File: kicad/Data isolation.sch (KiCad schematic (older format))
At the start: 0 parts

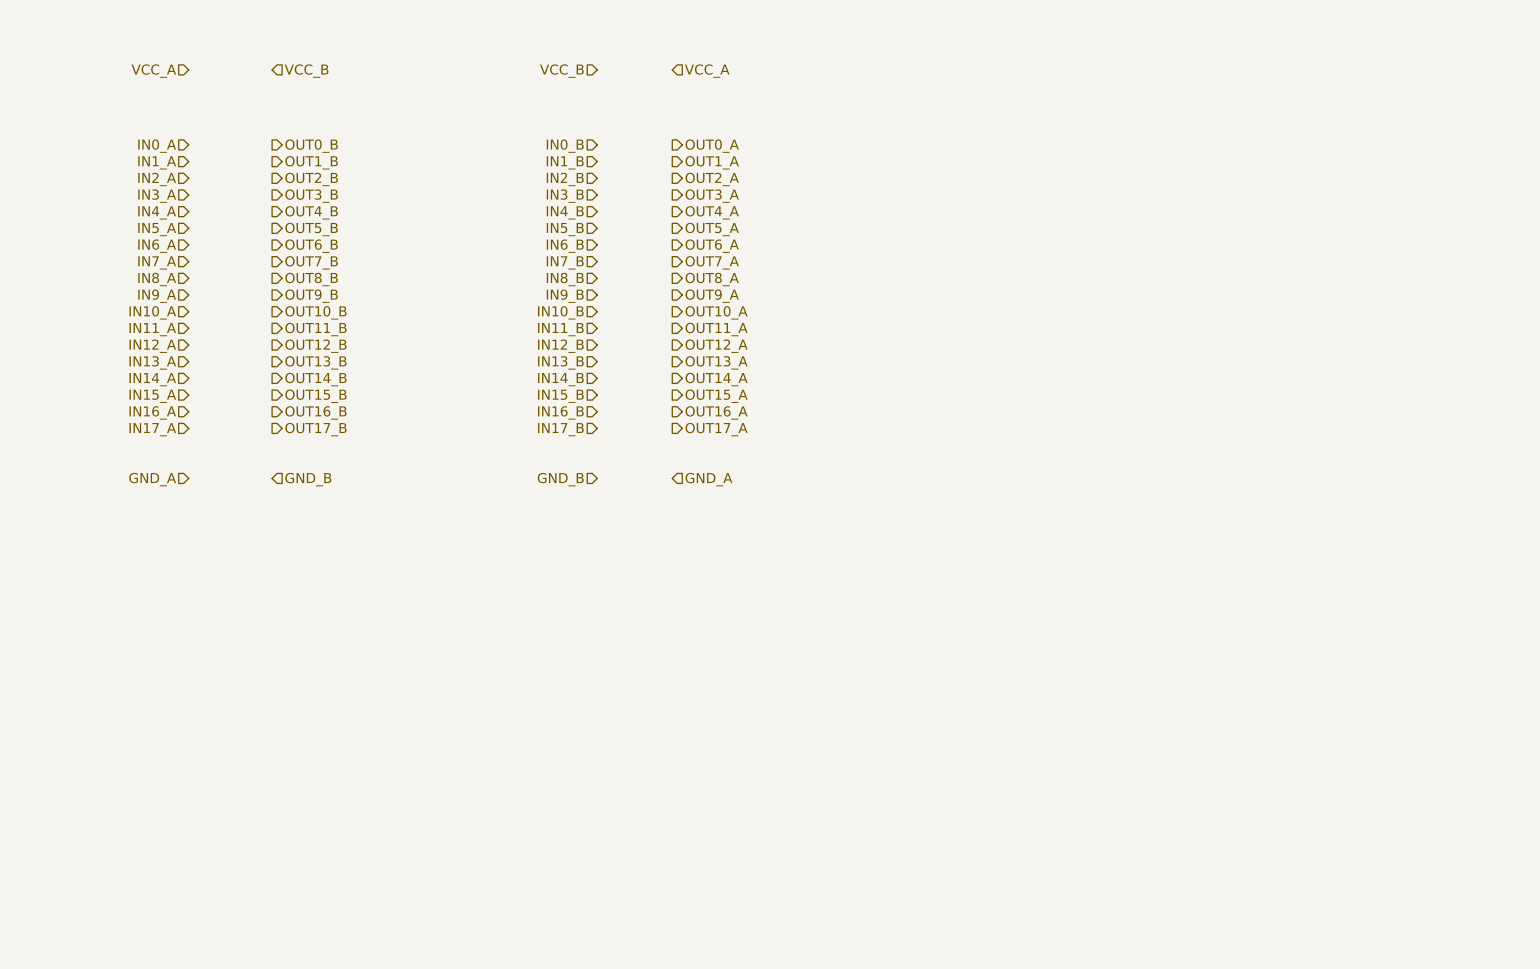
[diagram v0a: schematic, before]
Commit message: Completed data and power isolation sheets
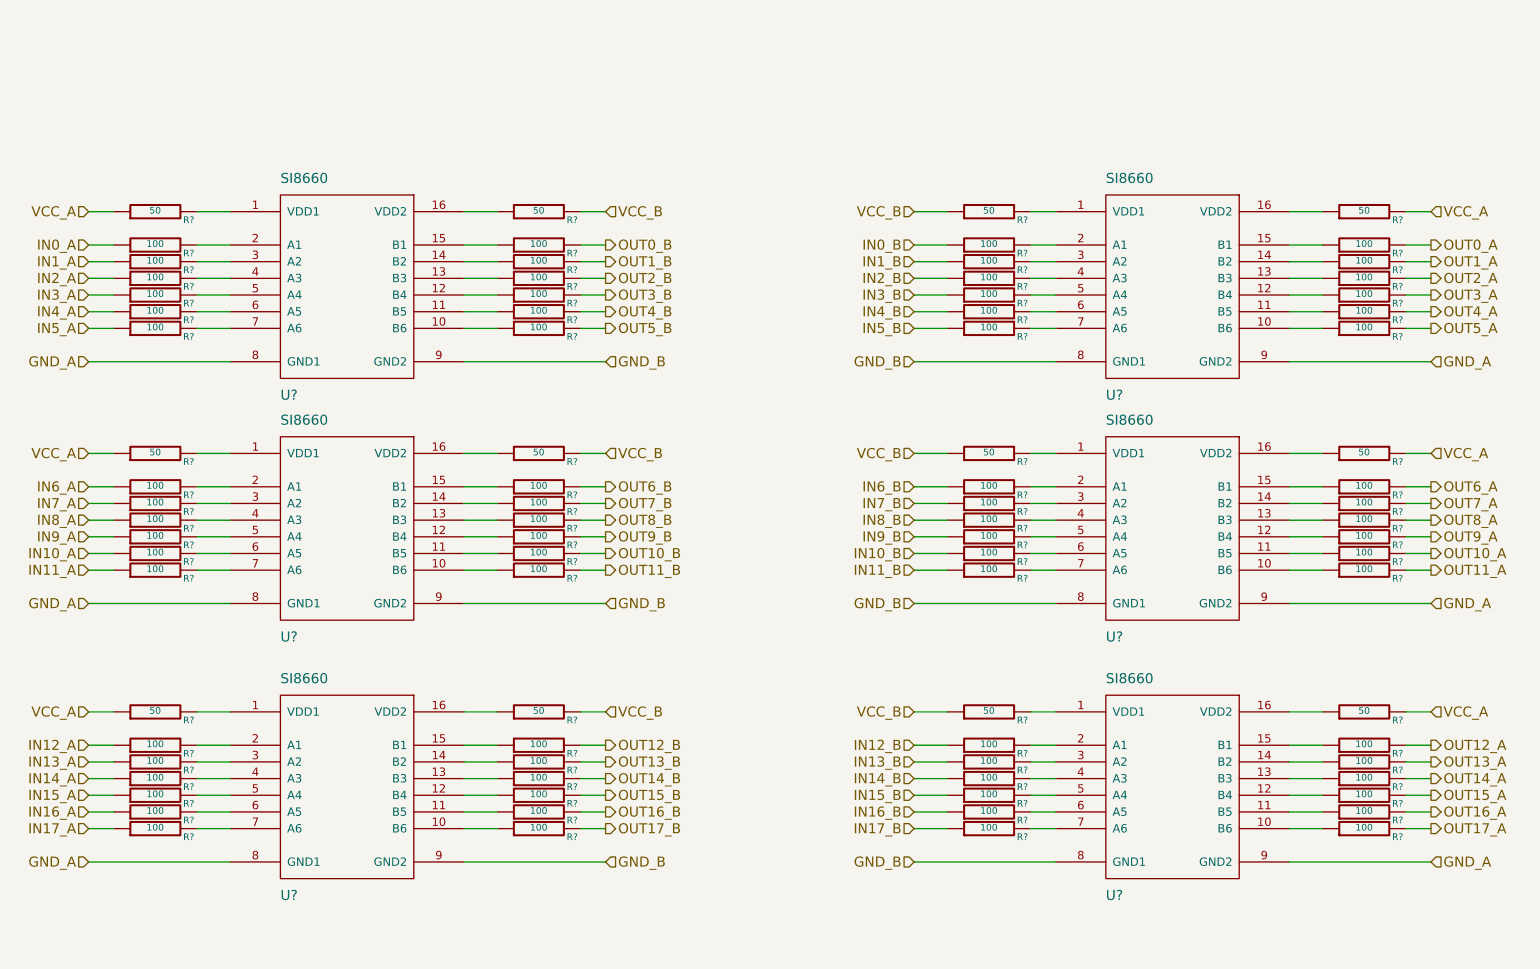
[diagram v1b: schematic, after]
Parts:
- added R? (x12): 50, ~, symbol R
- added R? (x72): 100, ~, symbol R
- added U? (x6): SI8660, ~, symbol SI8660
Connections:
- net GND_A: now also U?.8 (GND1), U?.8 (GND1), U?.8 (GND1), U?.9 (GND2), U?.9 (GND2), U?.9 (GND2)
- net GND_B: now also U?.8 (GND1), U?.8 (GND1), U?.8 (GND1), U?.9 (GND2), U?.9 (GND2), U?.9 (GND2)
- net IN0_A: now also R?.1
- net IN0_B: now also R?.1
- net IN10_A: now also R?.1
- net IN10_B: now also R?.1
- net IN11_A: now also R?.1
- net IN11_B: now also R?.1
- net IN12_A: now also R?.1
- net IN12_B: now also R?.1
- net IN13_A: now also R?.1
- net IN13_B: now also R?.1
- net IN14_A: now also R?.1
- net IN14_B: now also R?.1
- net IN15_A: now also R?.1
- net IN15_B: now also R?.1
- net IN16_A: now also R?.1
- net IN16_B: now also R?.1
- net IN17_A: now also R?.1
- net IN17_B: now also R?.1
- net IN1_A: now also R?.1
- net IN1_B: now also R?.1
- net IN2_A: now also R?.1
- net IN2_B: now also R?.1
- net IN3_A: now also R?.1
- net IN3_B: now also R?.1
- net IN4_A: now also R?.1
- net IN4_B: now also R?.1
- net IN5_A: now also R?.1
- net IN5_B: now also R?.1
- net IN6_A: now also R?.1
- net IN6_B: now also R?.1
- net IN7_A: now also R?.1
- net IN7_B: now also R?.1
- net IN8_A: now also R?.1
- net IN8_B: now also R?.1
- net IN9_A: now also R?.1
- net IN9_B: now also R?.1
- net OUT0_A: now also R?.2
- net OUT0_B: now also R?.2
- net OUT10_A: now also R?.2
- net OUT10_B: now also R?.2
- net OUT11_A: now also R?.2
- net OUT11_B: now also R?.2
- net OUT12_A: now also R?.2
- net OUT12_B: now also R?.2
- net OUT13_A: now also R?.2
- net OUT13_B: now also R?.2
- net OUT14_A: now also R?.2
- net OUT14_B: now also R?.2
- net OUT15_A: now also R?.2
- net OUT15_B: now also R?.2
- net OUT16_A: now also R?.2
- net OUT16_B: now also R?.2
- net OUT17_A: now also R?.2
- net OUT17_B: now also R?.2
- net OUT1_A: now also R?.2
- net OUT1_B: now also R?.2
- net OUT2_A: now also R?.2
- net OUT2_B: now also R?.2
- net OUT3_A: now also R?.2
- net OUT3_B: now also R?.2
- net OUT4_A: now also R?.2
- net OUT4_B: now also R?.2
- net OUT5_A: now also R?.2
- net OUT5_B: now also R?.2
- net OUT6_A: now also R?.2
- net OUT6_B: now also R?.2
- net OUT7_A: now also R?.2
- net OUT7_B: now also R?.2
- net OUT8_A: now also R?.2
- net OUT8_B: now also R?.2
- net OUT9_A: now also R?.2
- net OUT9_B: now also R?.2
- net VCC_A: now also R?.1, R?.1, R?.1, R?.2, R?.2, R?.2
- net VCC_B: now also R?.1, R?.1, R?.1, R?.2, R?.2, R?.2
- new net: R?.2, U?.1 (VDD1) (x6)
- new net: R?.1, U?.16 (VDD2) (x6)
- new net: R?.2, U?.2 (A1) (x6)
- new net: R?.2, U?.3 (A2) (x6)
- new net: R?.2, U?.4 (A3) (x6)
- new net: R?.2, U?.5 (A4) (x6)
- new net: R?.2, U?.6 (A5) (x6)
- new net: R?.2, U?.7 (A6) (x6)
- new net: R?.1, U?.15 (B1) (x6)
- new net: R?.1, U?.14 (B2) (x6)
- new net: R?.1, U?.13 (B3) (x6)
- new net: R?.1, U?.12 (B4) (x6)
- new net: R?.1, U?.11 (B5) (x6)
- new net: R?.1, U?.10 (B6) (x6)

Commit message: ID controller complete, bypass caps added in data isolation
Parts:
- added C? (x12): 0.1u, ~, symbol CSMALL
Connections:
- wire segments 180 -> 216
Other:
- moved on the sheet: R?, U?

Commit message: Netlist DRC pass - fixed pins types, incorrect connections, added PWRFLAGS
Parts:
- removed C? (x11): 0.1u, ~, symbol CSMALL
- added C602, C603, C604, C605, C606, C607, C608, C609, C610, C611, C612: 0.1u, ~, symbol CSMALL
- gave numbers to parts that had none: 91
